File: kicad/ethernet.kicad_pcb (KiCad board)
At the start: 2 copper layers, 92 x 62.5 mm, 107 parts, among them J1 RJ45_Abracon_ARJP11A-MASA-B-A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, J2 Conn_Coaxial, J3 JTAG, J4 BATT, J5 Conn_Coaxial, J6 Conn_Coaxial, J7 POE, J8 POE+, J9 POE-, Q1 3904, Q10 3904, Q11 3904, Q12 3906, Q13 3904, Q2 3904, Q3 BSC340N08NS3G, Q4 MMBT5401L, Q5 3904, Q6 3906, Q7 3904, Q8 3906, Q9 3904, SW1 KSC701, U1 MSP432E401Y, U2 MAX-8Q, U3 TLV75733PDRV, U4 74AUC2G34, U5 74AUC2G34, U6 LT1634BCMS8-2.5, U7 4N25, Y1 NX3225GA-25.000M-STD-CRG-2

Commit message: board layout update
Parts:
- added C32: 10u, Capacitor_SMD:C_0805_2012Metric, F.Cu at (126.0, 88.2)
- added C33: 100n, Capacitor_SMD:C_0805_2012Metric, F.Cu at (122.0, 89.0)
- added C34: 100n, Capacitor_SMD:C_0805_2012Metric, F.Cu at (129.8, 90.8)
- C29, C30: footprint Capacitor_SMD:C_0805_2012Metric -> Capacitor_SMD:C_1210_3225Metric
- D9: value RB168L100DDTE25 -> RB068L100TE25
- R21: value 4.7k -> 10k
- R31: value 100 -> 330
- R34: value 10k -> 3k
- R7: value 2.5k -> 3k
- moved R32 3.40 mm to (57.8, 91.8), turned to -90 degrees
- moved Q5 3.25 mm to (73.2, 81.0)
- moved Q6 3.25 mm to (69.8, 81.0)
- moved Q8 3.25 mm to (73.2, 85.2)
- moved Q9 3.25 mm to (69.8, 85.2)
- moved R28 3.25 mm to (71.5, 88.5)
- moved R29 3.16 mm to (67.8, 88.5)
- moved C28 3.01 mm to (74.0, 92.0)
- moved Q10 3.00 mm to (71.0, 91.8)
- moved Q11 3.00 mm to (65.0, 91.8)
- moved R30 3.00 mm to (68.0, 91.8)
- moved R34 3.00 mm to (64.0, 88.5), turned to 180 degrees
- moved R4 3.00 mm to (123.0, 92.5)
- moved Q12 2.50 mm to (60.8, 91.8), turned to 0 degrees
- moved R31 2.45 mm to (52.8, 88.2), turned to 180 degrees
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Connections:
- net Net-(D9-Pad2) renamed /RECT
- Q12 pad 3: Net-(Q12-Pad3) -> Net-(R34-Pad2)
- R12 pad 1: Net-(Q2-Pad1) -> +BATT
- R12 pad 2: +BATT -> Net-(Q2-Pad1)
- R34 pad 1: Net-(Q12-Pad3) -> Net-(Q9-Pad1)
- R34 pad 2: Net-(Q9-Pad1) -> Net-(R34-Pad2)
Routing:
- net +BATT: track 17.5 -> 4.08 mm
- net -POE: track 10.2 -> 0.00 mm, vias 26 -> 28
- net Net-(Q9-Pad1): track 18.3 -> 24.1 mm
- net /VDRV: track 5.19 -> 0.00 mm
- net Net-(R34-Pad2): track 0.00 -> 4.16 mm
- net /RECT: track 3.78 -> 0.00 mm
- net /ISENSE: track 12.1 -> 15.7 mm
- net Net-(Q12-Pad3): track 3.07 -> 0.00 mm
- net ETH_LED0: track 29.2 -> 31.1 mm
- net Net-(D8-Pad1): track 7.79 -> 5.95 mm
- net ETH_LED1: track 26.9 -> 28.8 mm
- net +3V3: track 26.9 -> 25.1 mm, vias 9 -> 7
- net Net-(Q4-Pad1): track 2.44 -> 4.13 mm
- net Net-(Q3-Pad4): track 14.8 -> 16.2 mm
- net Net-(Q12-Pad1): track 41.2 -> 39.8 mm
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- added copper zone on F.Cu, net /RECT
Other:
- board text added: "+"

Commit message: board layout update
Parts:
- added C35: 100n, Capacitor_SMD:C_0805_2012Metric, F.Cu at (124.8, 75.0)
- moved R11 2.16 mm to (124.8, 66.0)
- moved C1 0.35 mm to (118.2, 67.8)
- moved C15 0.35 mm to (119.8, 69.2)
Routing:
- net +3V3: track 25.1 -> 17.2 mm
- net GND: track 29.6 -> 23.5 mm, vias 94 -> 99
- net ~{RST}: track 36.6 -> 34.8 mm
- net Net-(C1-Pad1): track 6.39 -> 5.63 mm

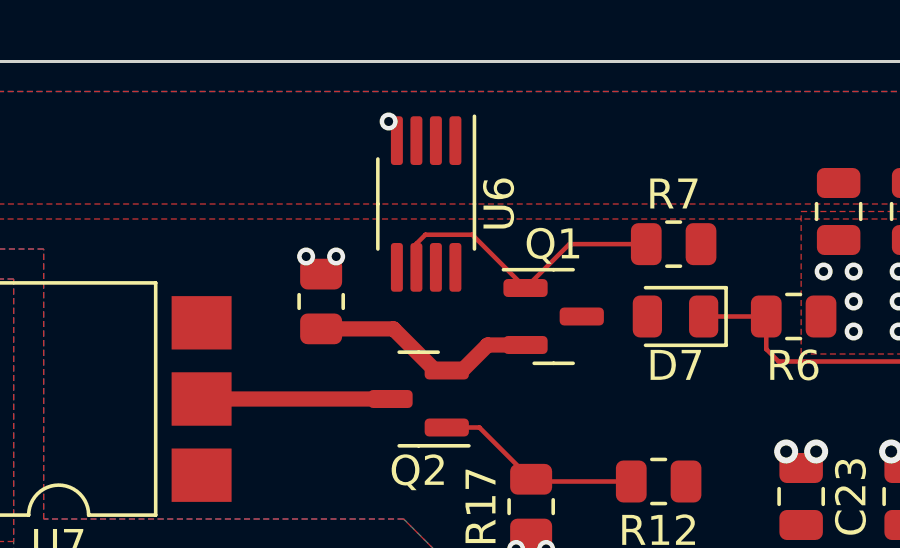
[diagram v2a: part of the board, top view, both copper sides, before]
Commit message: update schematic
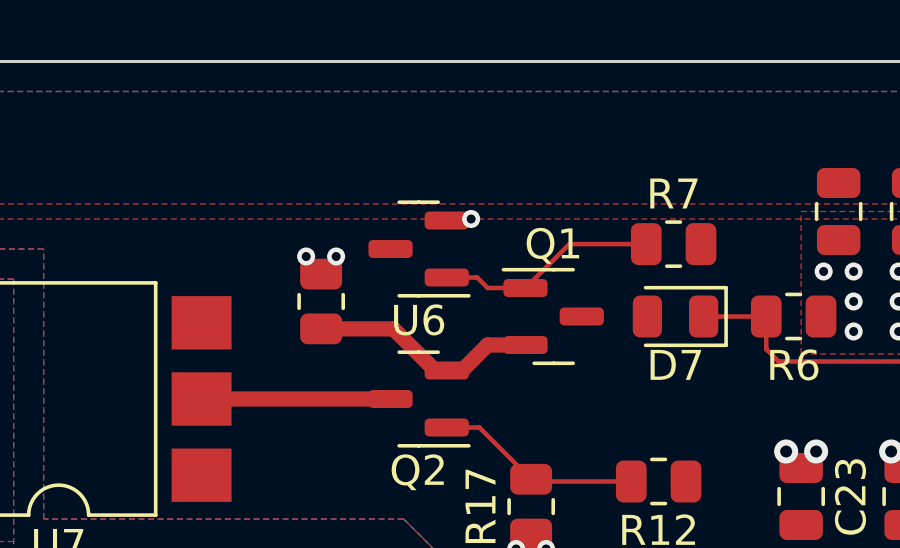
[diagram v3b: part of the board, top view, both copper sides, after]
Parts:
- U6: value LT1634BCMS8-2.5 -> LM4040DBZ-2.5; footprint Package_SO:MSOP-8_3x3mm_P0.65mm -> Package_TO_SOT_SMD:SOT-23
- moved U6 1.52 mm to (69.5, 56.2), turned to 180 degrees
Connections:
- U6 pad 1: (no net) -> Net-(Q1-Pad1)
- U6 pad 2: (no net) -> GND
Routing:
- net Net-(Q1-Pad1): track 9.92 -> 7.40 mm

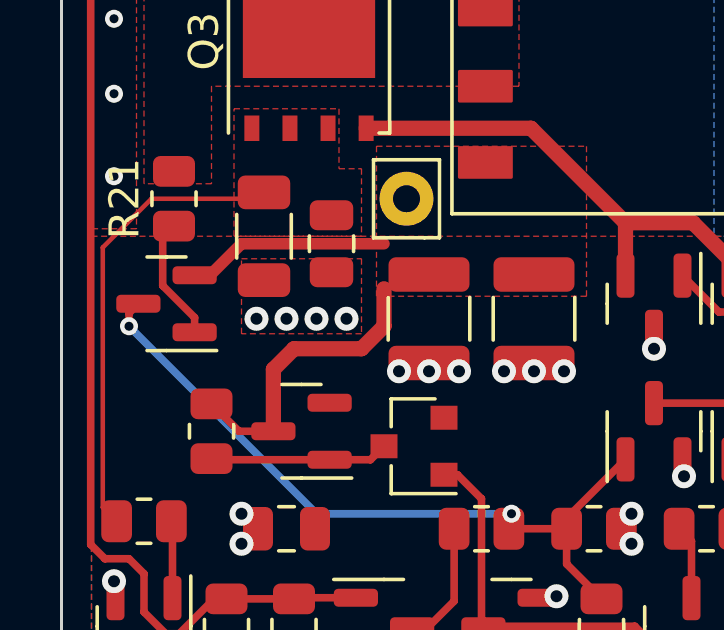
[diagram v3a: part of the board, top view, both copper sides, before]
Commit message: migrating to C++
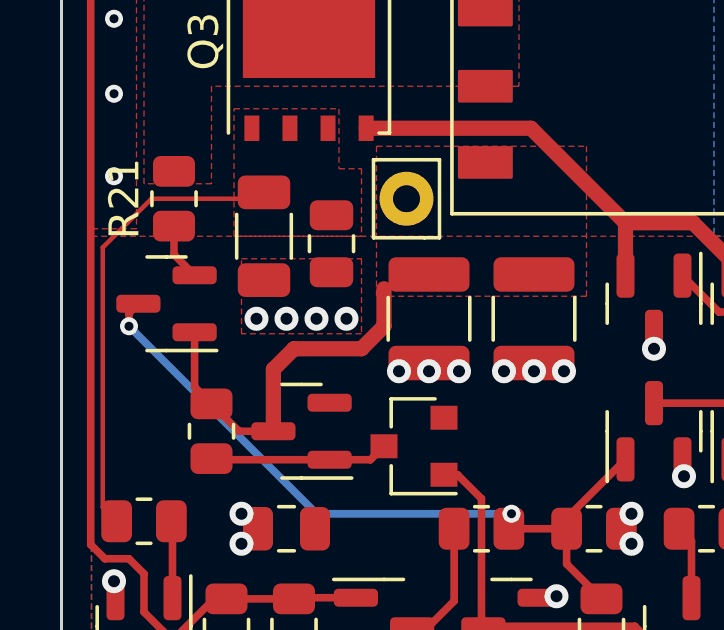
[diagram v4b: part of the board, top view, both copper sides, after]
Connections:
- Q4 pad 1: Net-(Q4-Pad1) -> +POE
- Q4 pad 2: +POE -> Net-(Q4-Pad2)
- R21 pad 1: Net-(Q4-Pad1) -> Net-(Q4-Pad2)
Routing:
- net Net-(Q4-Pad1): track 4.13 -> 0.00 mm
- net +POE: track 16.8 -> 12.7 mm
- net Net-(Q4-Pad2): track 0.00 -> 2.43 mm
